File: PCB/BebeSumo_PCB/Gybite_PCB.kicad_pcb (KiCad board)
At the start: 2 copper layers, 77.7 x 36.4 mm, 15 parts, among them J1 Pulsador, J10 JSUMO, J11 Sharps, J12 Conector Batería, J2 Motor 1, J3 HC-SR04, J4 Motor 2, J5 QRE1113, J6 QRE1113, J7 Arduino_Nano_Header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

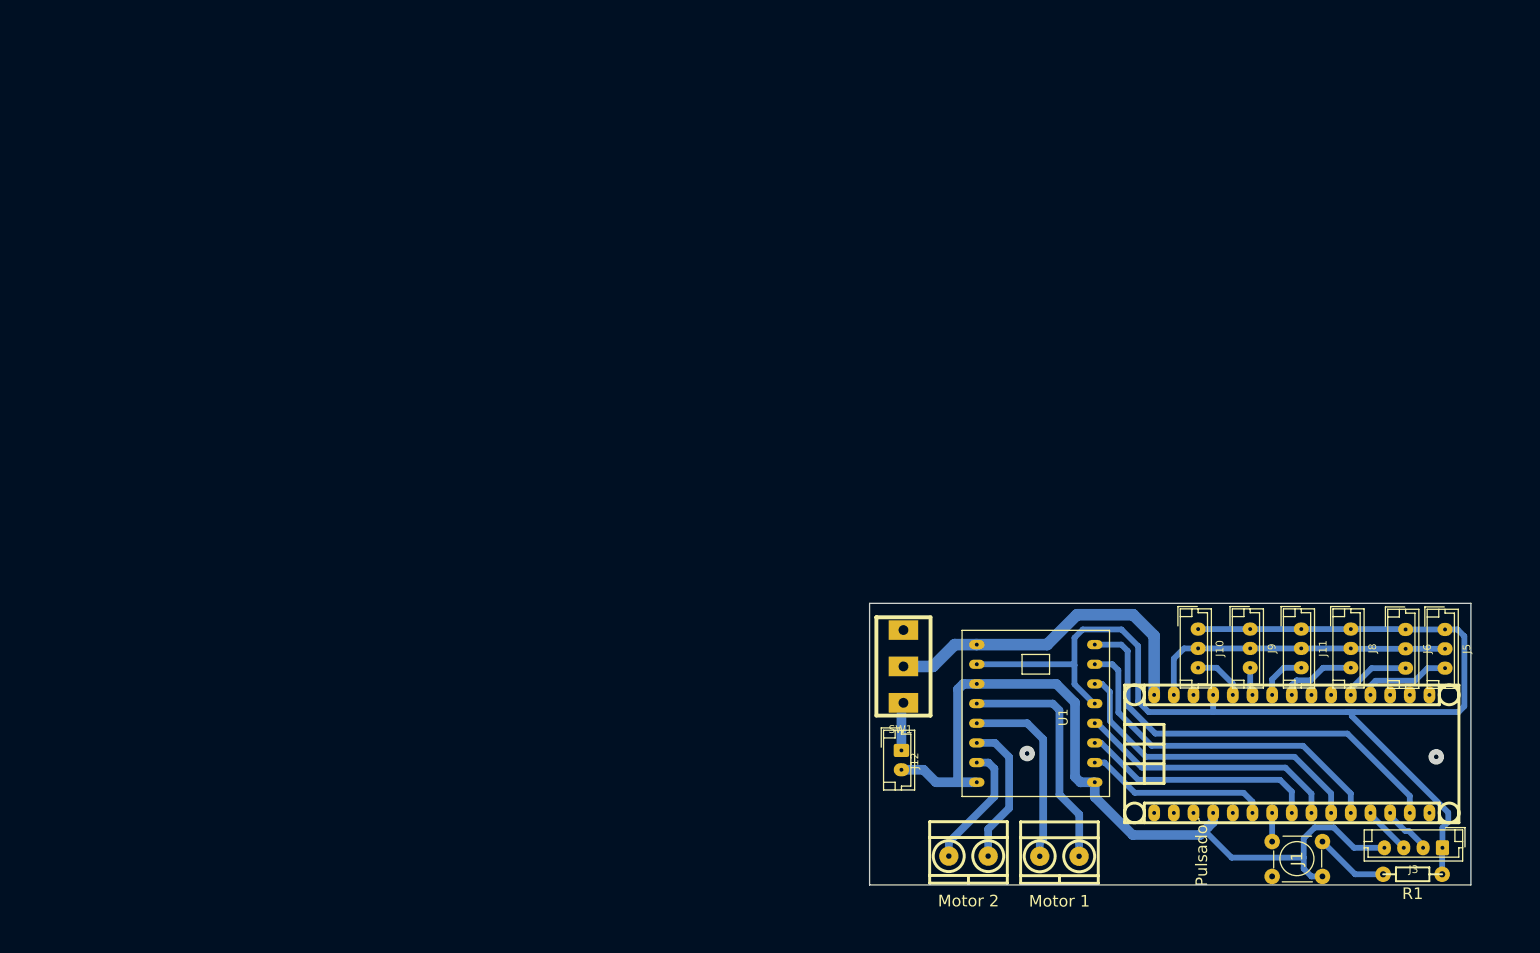
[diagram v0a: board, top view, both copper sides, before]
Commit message: Rediseño de la placa, ahora tiene un dip y la huella para el nuevo interruptor de corriente.
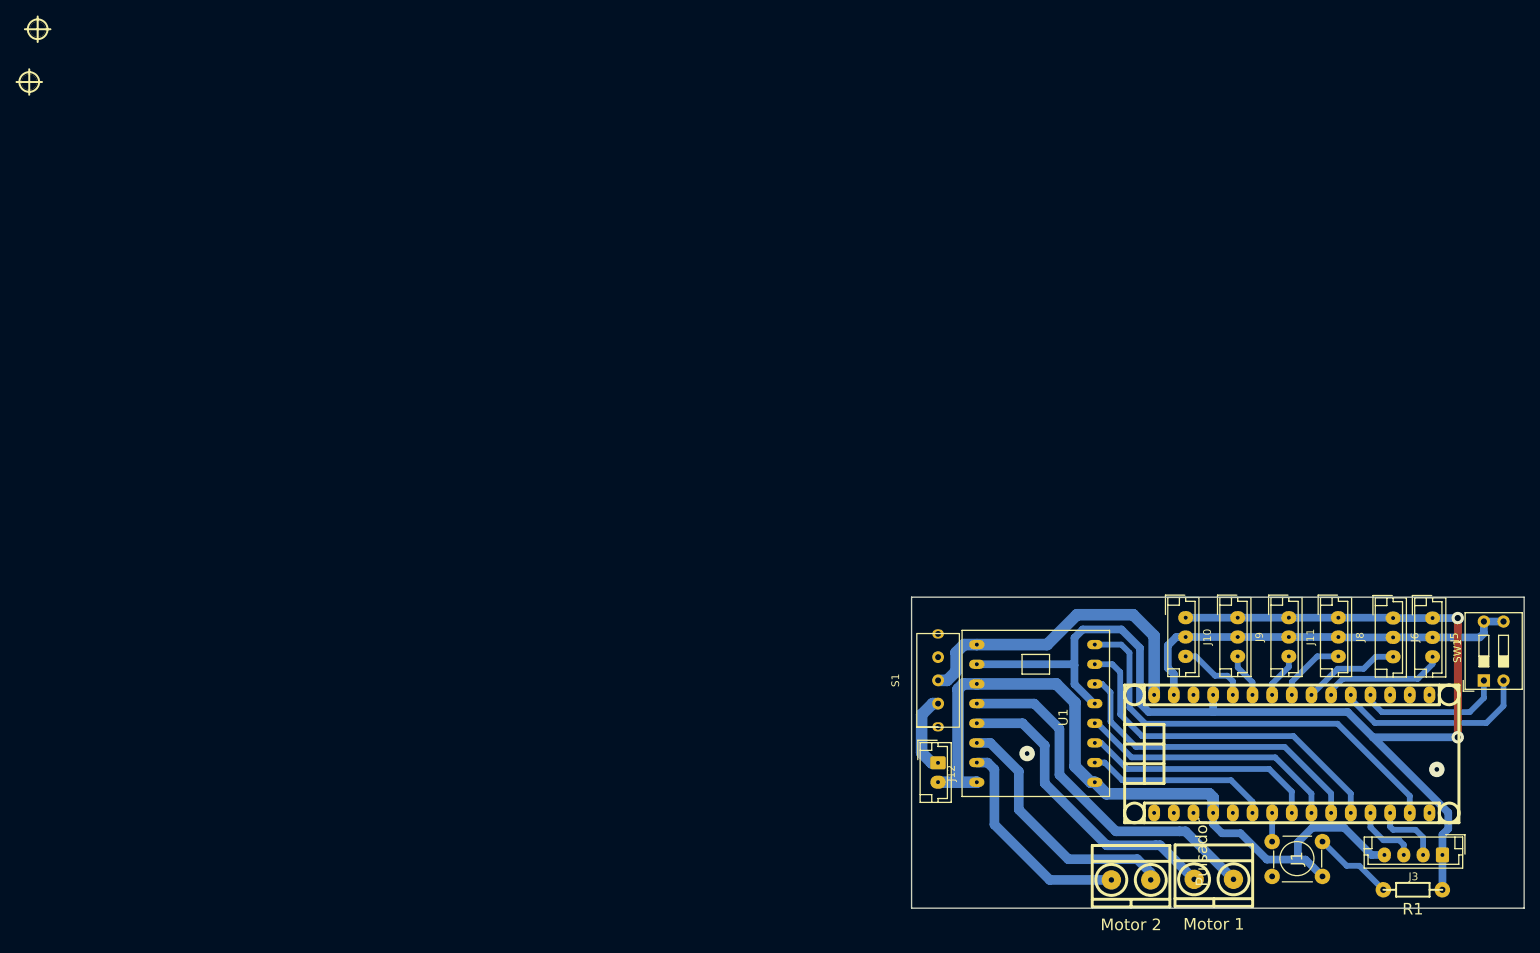
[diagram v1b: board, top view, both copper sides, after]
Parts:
- added H1: Mounting_Hole, EESTN5:hole_2mm, F.Cu at (4.22, 2.69)
- added H2: Mounting_Hole, EESTN5:hole_2mm, F.Cu at (3.13, 9.51)
- added S1: MINI-SPDT-SW, Switch.prety:Switch_SS12F44_123, F.Cu at (115.5, 86.8)
- SW1: value SW_SPDT -> SW_DIP_x02; footprint EESTN5:SW_SPDT_TH_Vertical -> Button_Switch_THT:SW_DIP_SPSTx02_Slide_9.78x7.26mm_W7.62mm_P2.54mm
- moved SW1 75.0 mm to (191.0, 86.8), turned to 90 degrees
- moved J4 21.2 mm to (145.4, 112.6)
- moved J2 20.2 mm to (156.1, 112.5)
- moved J12 4.99 mm to (120.5, 97.5)
- moved J10 2.18 mm to (152.5, 78.7)
- moved J8 2.18 mm to (172.2, 78.7)
- moved J9 2.18 mm to (159.2, 78.7)
- moved J11 2.18 mm to (165.8, 78.7)
- moved J5 2.18 mm to (184.4, 78.8)
- moved J6 2.18 mm to (179.3, 78.8)
- moved R1 2.00 mm to (181.8, 113.8)
- moved J3 0.92 mm to (185.7, 109.3)
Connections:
- net /A4 renamed /JSUMO_Izq
- net /A5 renamed /Sharp_Izq
- net /A6 renamed /Sharp_Der
- net /A7 renamed /JSUMO_Der
- J5 pad 3: /CNY_DER -> /QRE_DER
- J6 pad 3: /CNY_IZQ -> /QRE_IZQ
- J7 pad 19: /CNY_DER -> /Salida_0
- J7 pad 20: /CNY_IZQ -> /Salida_1
- J7 pad 21: unconnected-(J7-Pad21) -> /QRE_DER
- J7 pad 22: unconnected-(J7-Pad22) -> /QRE_IZQ
- SW1 pad 1: +BATT -> /Salida_0
- SW1 pad 2: VCC -> /Salida_1
- SW1 pad 3: unconnected-(SW1-Pad3) -> GND
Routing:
- net /Salida_1: track 0.00 -> 25.7 mm
- net /Salida_0: track 0.00 -> 19.0 mm
- net /QRE_DER: track 0.00 -> 16.0 mm
- net /Motor 1A: track 31.0 -> 46.0 mm
- net /Motor 1B: track 24.7 -> 39.3 mm
- net /Motor 2A: track 18.8 -> 33.2 mm
- net /QRE_IZQ: track 0.00 -> 12.7 mm
- net /CNY_DER: track 11.8 -> 0.00 mm
- net /Motor 2B: track 16.3 -> 27.8 mm
- net /CNY_IZQ: track 8.96 -> 0.00 mm
- net +BATT: track 6.26 -> 10.3 mm
- net GND: track 145.8 -> 149.5 mm
- net +5V: track 155.4 -> 159.1 mm, vias 0 -> 2
- net /JSUMO_Der: track 6.79 -> 9.23 mm
- net /Pin_Echo: track 6.53 -> 8.89 mm
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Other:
- board size 77.7 x 36.4 mm -> 79.1 x 40.2 mm
